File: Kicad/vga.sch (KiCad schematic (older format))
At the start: 7 parts, among them J901 DB15HD_Female

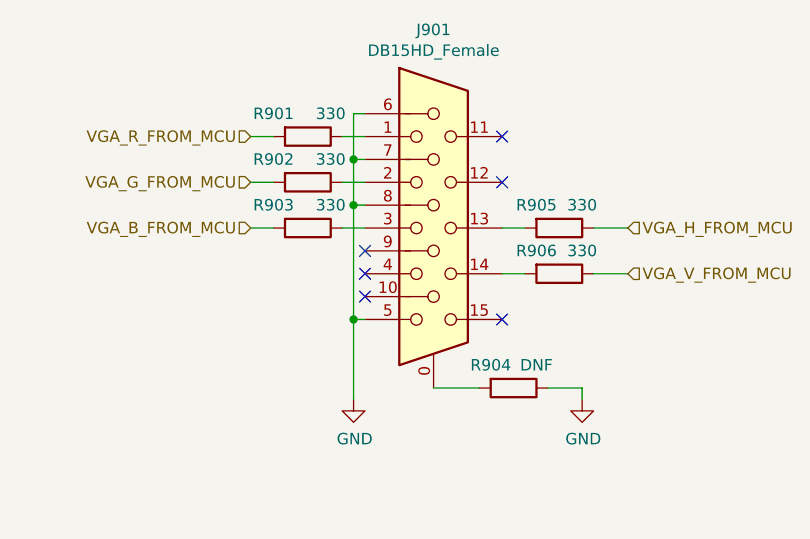
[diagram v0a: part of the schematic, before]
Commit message: Switch to 1598D enclosure.
Use MIC2005A current limiter on input.
Use soft on/off switch from Atmega.
Atmega connects to Tiva over I2C.
Use full-size SD card.
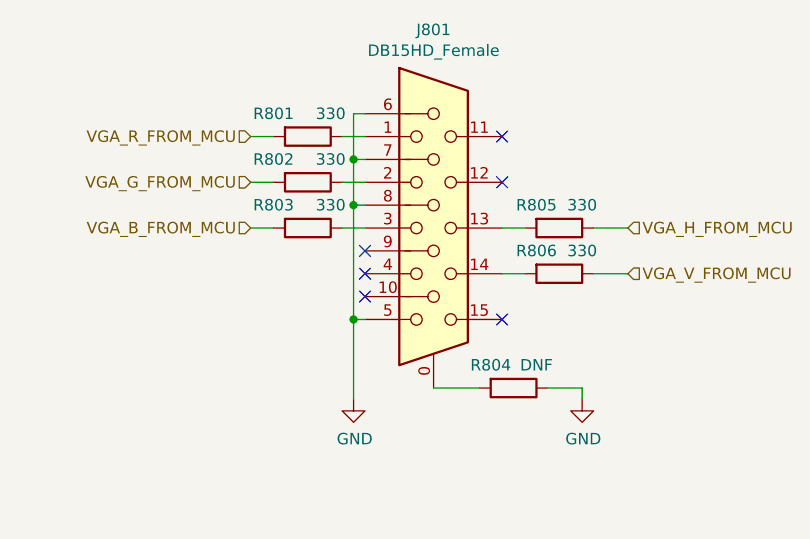
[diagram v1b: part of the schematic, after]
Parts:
- renumbered J901 to J801, R901 to R801, R902 to R802, R903 to R803, R904 to R804, R905 to R805, R906 to R806
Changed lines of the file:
@@
 $Descr A4 11693 8268
 encoding utf-8
-Sheet 9 10
+Sheet 8 12
 Title "Neotron 32K Main PCB"
 Date "2020-03-29"
@@
 P 5550 3250
 AR Path="/5DF388AB" Ref="J?"  Part="1"
-AR Path="/5DF25A09/5DF388AB" Ref="J901"  Part="1"
-F 0 "J901" H 5550 4117 50  0000 C CNN
+AR Path="/5DF25A09/5DF388AB" Ref="J801"  Part="1"
+F 0 "J801" H 5550 4117 50  0000 C CNN
 F 1 "DB15HD_Female" H 5550 4026 50  0000 C CNN
 F 2 "Connector_Dsub:DSUB-15-HD_Female_Horizontal_P2.29x1.98mm_EdgePinOffset3.03mm_Housed_MountingHolesOffset4.94mm" H 4600 3650 50  0001 C CNN
@@
 VGA_V_FROM_MCU
 $Comp
-L Device:R R906
+L Device:R R806
 U 1 1 5E020EF6
 P 6100 3450
-F 0 "R906" V 6000 3350 50  0000 C CNN
+F 0 "R806" V 6000 3350 50  0000 C CNN
 F 1 "330" V 6000 3550 50  0000 C CNN
 F 2 "Resistor_THT:R_Axial_DIN0207_L6.3mm_D2.5mm_P10.16mm_Horizontal" V 6030 3450 50  0001 C CNN
@@
 $EndComp
 $Comp
-L Device:R R905
+L Device:R R805
 U 1 1 5E02143C
 P 6100 3250
-F 0 "R905" V 6000 3150 50  0000 C CNN
+F 0 "R805" V 6000 3150 50  0000 C CNN
 F 1 "330" V 6000 3350 50  0000 C CNN
 F 2 "Resistor_THT:R_Axial_DIN0207_L6.3mm_D2.5mm_P10.16mm_Horizontal" V 6030 3250 50  0001 C CNN
@@
 $EndComp
 $Comp
-L Device:R R901
+L Device:R R801
 U 1 1 5E021698
 P 5000 2850
-F 0 "R901" V 4900 2700 50  0000 C CNN
+F 0 "R801" V 4900 2700 50  0000 C CNN
 F 1 "330" V 4900 2950 50  0000 C CNN
 F 2 "Resistor_THT:R_Axial_DIN0207_L6.3mm_D2.5mm_P10.16mm_Horizontal" V 4930 2850 50  0001 C CNN
@@
 $EndComp
 $Comp
-L Device:R R902
+L Device:R R802
 U 1 1 5E021BC3
 P 5000 3050
-F 0 "R902" V 4900 2900 50  0000 C CNN
+F 0 "R802" V 4900 2900 50  0000 C CNN
 F 1 "330" V 4900 3150 50  0000 C CNN
 F 2 "Resistor_THT:R_Axial_DIN0207_L6.3mm_D2.5mm_P10.16mm_Horizontal" V 4930 3050 50  0001 C CNN
@@
 $EndComp
 $Comp
-L Device:R R903
+L Device:R R803
 U 1 1 5E021E5E
 P 5000 3250
-F 0 "R903" V 4900 3100 50  0000 C CNN
+F 0 "R803" V 4900 3100 50  0000 C CNN
 F 1 "330" V 4900 3350 50  0000 C CNN
 F 2 "Resistor_THT:R_Axial_DIN0207_L6.3mm_D2.5mm_P10.16mm_Horizontal" V 4930 3250 50  0001 C CNN
@@
 $EndComp
 $Comp
-L Device:R R904
+L Device:R R804
 U 1 1 5E3BC4C1
 P 5900 3950
-F 0 "R904" V 5800 3850 50  0000 C CNN
+F 0 "R804" V 5800 3850 50  0000 C CNN
 F 1 "DNF" V 5800 4050 50  0000 C CNN
 F 2 "Resistor_THT:R_Axial_DIN0207_L6.3mm_D2.5mm_P10.16mm_Horizontal" V 5830 3950 50  0001 C CNN
